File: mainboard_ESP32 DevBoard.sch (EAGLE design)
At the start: 42 parts, among them IC1 OP-AMP-2-LONG, IC2 OP-AMP-2-LONG, IC3 74HC08N, K1 AQH213, X1 JST-XH-02-PIN-LONG-PAD, X2 JST-XH-04-PIN-LONG-PAD, X3 1751248, X4 1751248, X5 JST-XH-04-PIN-LONG-PAD

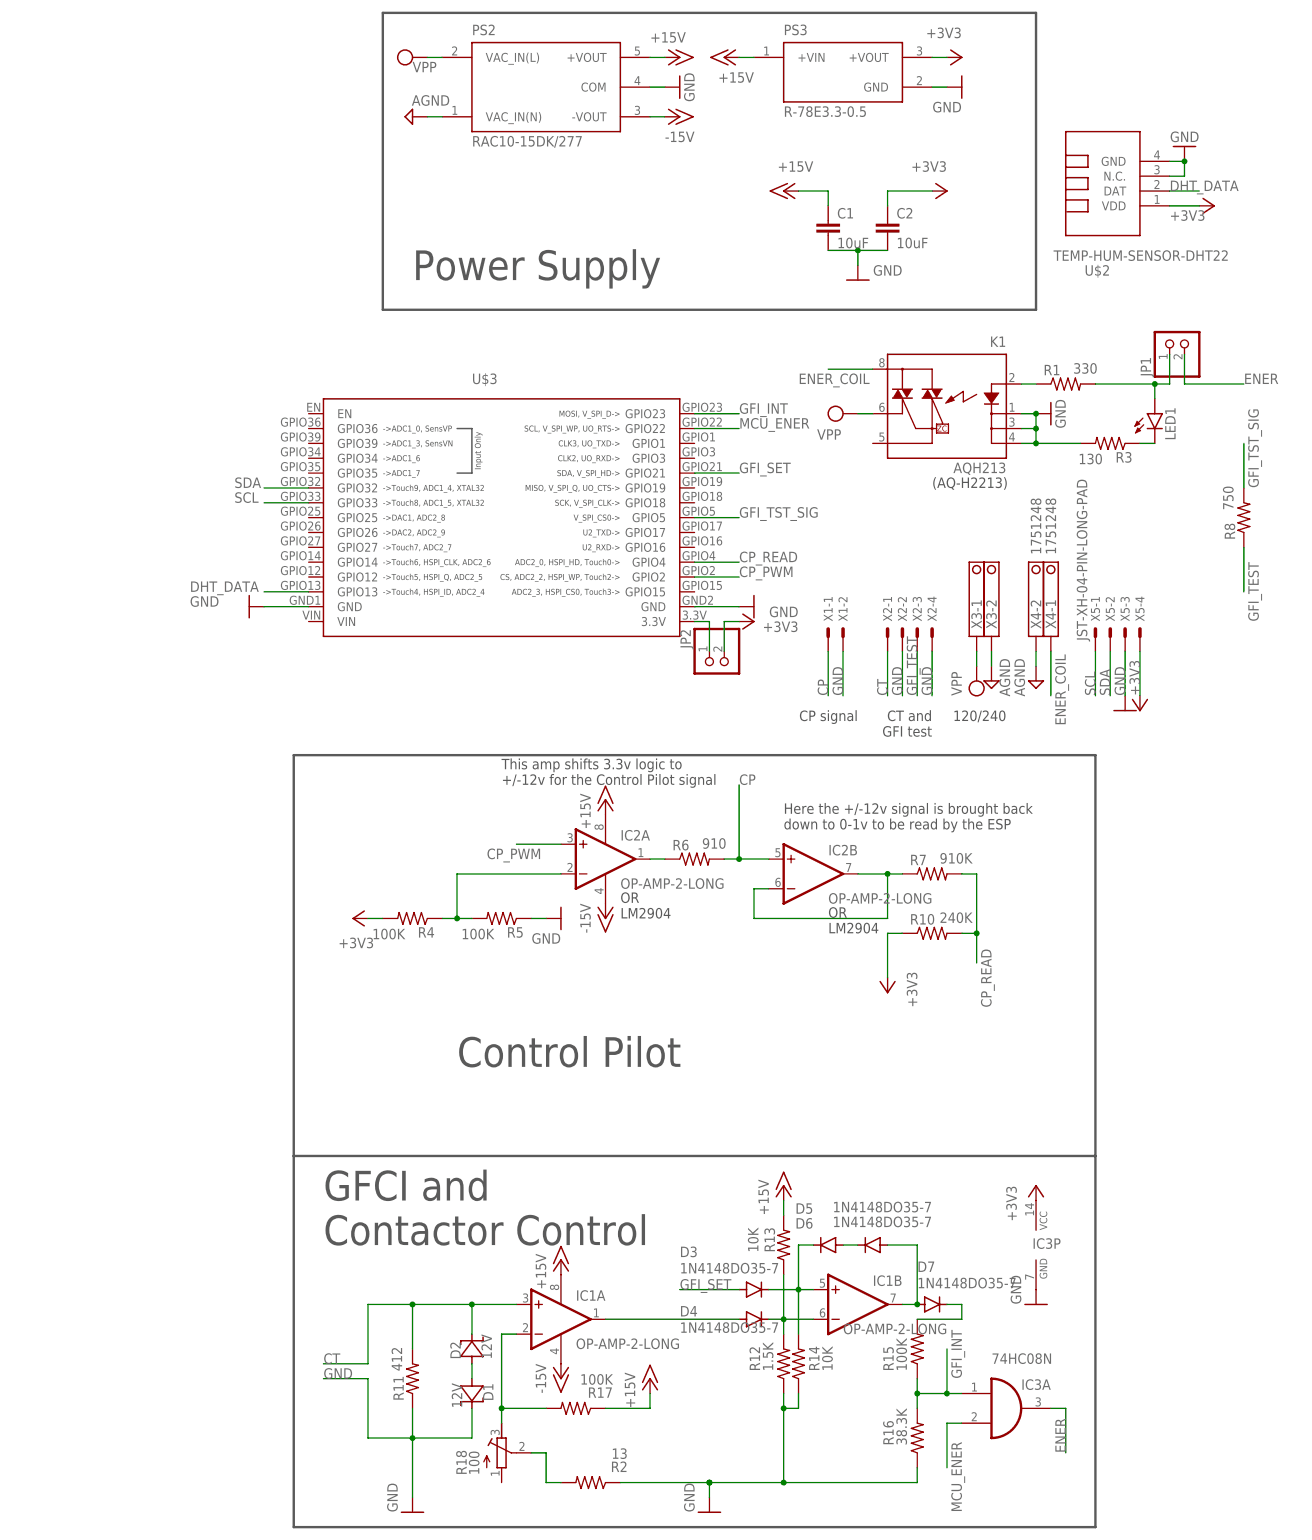
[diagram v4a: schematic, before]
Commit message: Updated ignore file. Made some adjustments after making the first board.
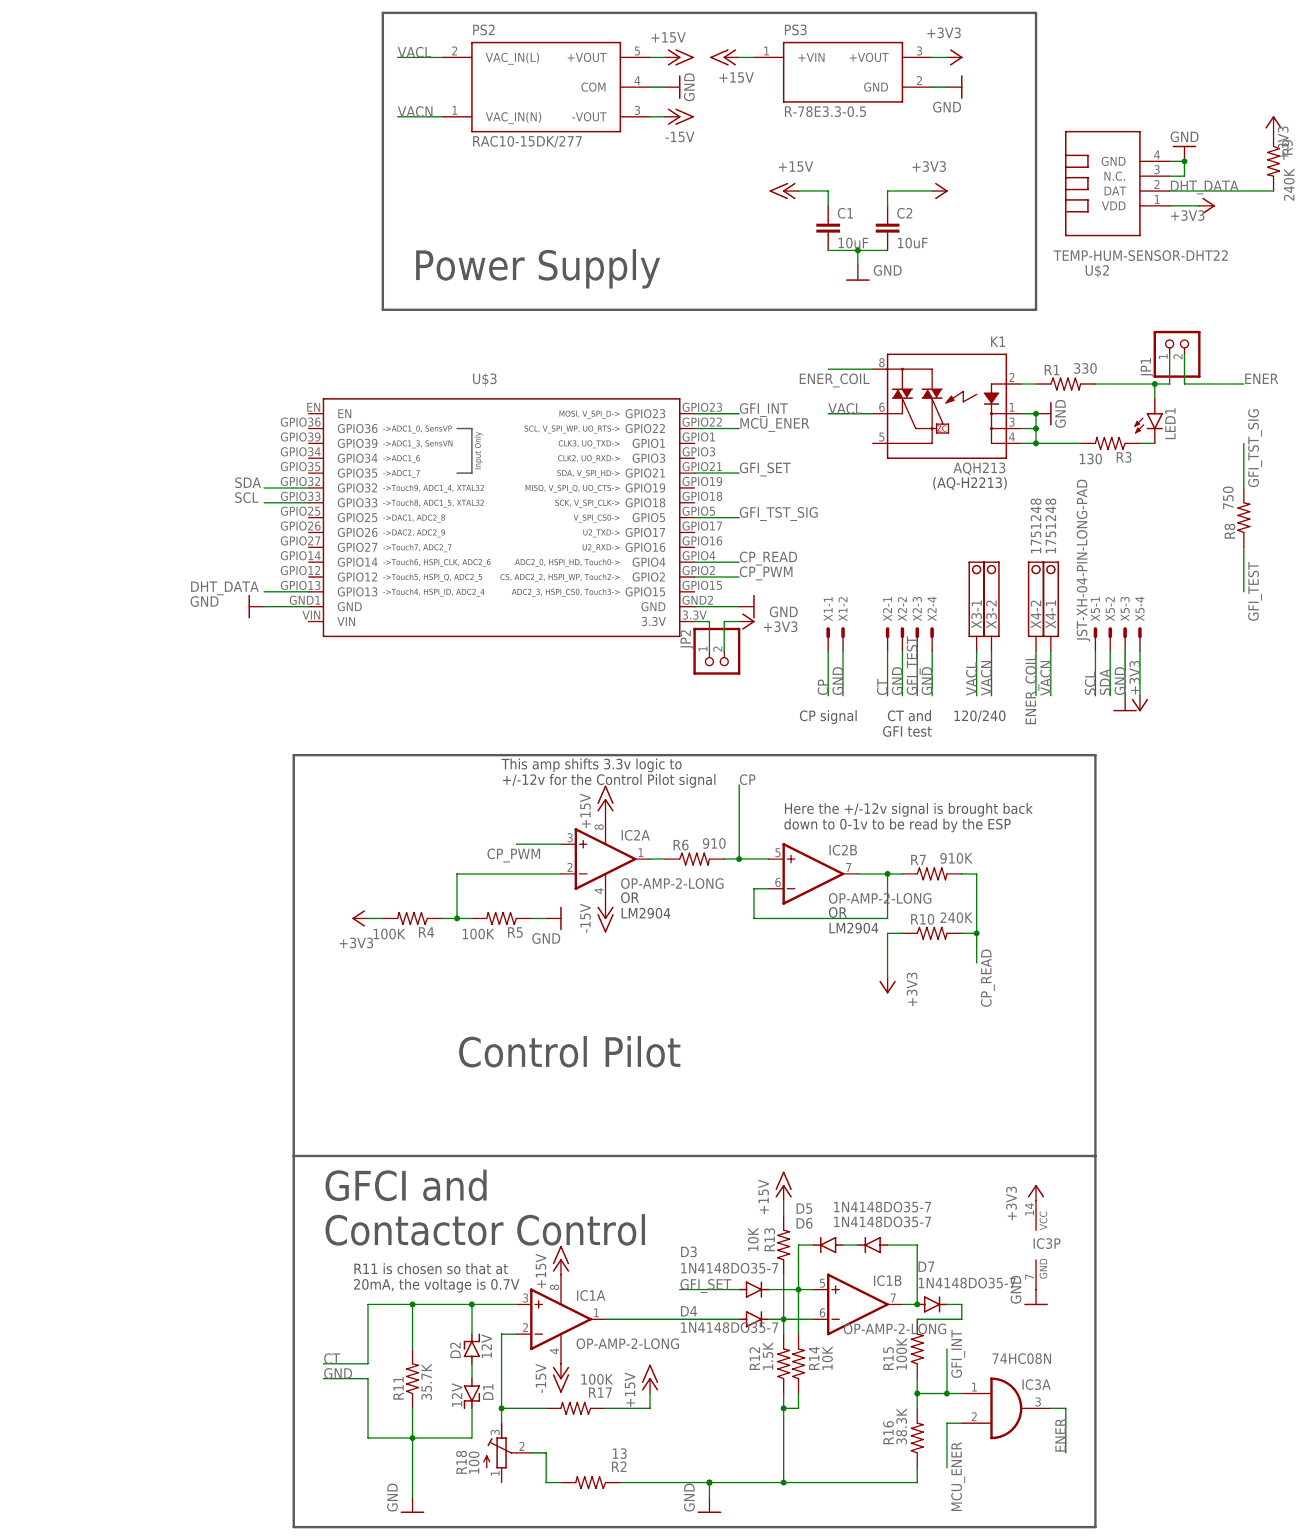
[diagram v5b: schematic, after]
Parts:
- added R9: 240K, Passive:RESISTORL
- R11: value 412 -> 35.7K
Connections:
- net VPP renamed VACL
- removed net AGND: PS2.VAC_IN(N), X3-2.K, X4-2.K
- new net VACN: PS2.VAC_IN(N), X3-2.K, X4-1.K
- net +3V3: now also R9.1
- net DHT_DATA: now also R9.2
- net ENER_COIL: now also X4-2.K; no longer X4-1.K
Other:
- note added: "R11 is chosen so that at 20mA, the voltage is 0.7V"
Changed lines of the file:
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@@
 <class number="0" name="default" width="0" drill="0">
+</class>
+<class number="1" name="Mains" width="0" drill="0">
+<clearance class="1" value="1.2"/>
 </class>
 </classes>
 <parts>
 <part name="K1" library="relay" library_urn="urn:adsk.eagle:library:339" deviceset="AQH*213" device="" package3d_urn="urn:adsk.eagle:package:24378/1" value="AQH213"/>
-<part name="SUPPLY1" library="supply2" library_urn="urn:adsk.eagle:library:372" deviceset="VPP" device=""/>
-<part name="SUPPLY2" library="supply2" library_urn="urn:adsk.eagle:library:372" deviceset="AGND" device=""/>
 <part name="R1" library="Passive" deviceset="RESISTOR" device="L" value="330"/>
 <part name="U$2" library="diy-modules" deviceset="TEMP-HUM-SENSOR-DHT22" device=""/>
@@
 <part name="PS2" library="RAC10-15DK_277" deviceset="RAC10-15DK/277" device=""/>
 <part name="GND10" library="supply1" library_urn="urn:adsk.eagle:library:371" deviceset="GND" device=""/>
-<part name="SUPPLY7" library="supply2" library_urn="urn:adsk.eagle:library:372" deviceset="VPP" device=""/>
-<part name="SUPPLY8" library="supply2" library_urn="urn:adsk.eagle:library:372" deviceset="AGND" device=""/>
 <part name="PS3" library="R-78E3.3-0.5" deviceset="R-78E3.3-0.5" device=""/>
 <part name="+3V5" library="supply1" library_urn="urn:adsk.eagle:library:371" deviceset="+3V3" device=""/>
@@
 <part name="D2" library="Passive" deviceset="ZENER" device="" value="12V"/>
 <part name="IC1" library="Op Amp" deviceset="OP-AMP-2" device="-LONG"/>
-<part name="R11" library="Passive" deviceset="RESISTOR" device="L" value="412"/>
+<part name="R11" library="Passive" deviceset="RESISTOR" device="L" value="35.7K"/>
 <part name="D3" library="diode" library_urn="urn:adsk.eagle:library:210" deviceset="1N4148" device="DO35-7" package3d_urn="urn:adsk.eagle:package:43339/2"/>
 <part name="D4" library="diode" library_urn="urn:adsk.eagle:library:210" deviceset="1N4148" device="DO35-7" package3d_urn="urn:adsk.eagle:package:43339/2"/>
@@
 <part name="X2" library="Rembrandt Electronics - JST XH Connectors v1-0" deviceset="JST-XH-04-PIN" device="-LONG-PAD"/>
 <part name="X3" library="con-phoenix-350" library_urn="urn:adsk.eagle:library:174" deviceset="1751248" device="" package3d_urn="urn:adsk.eagle:package:9395/1"/>
-<part name="SUPPLY5" library="supply2" library_urn="urn:adsk.eagle:library:372" deviceset="VPP" device=""/>
-<part name="SUPPLY6" library="supply2" library_urn="urn:adsk.eagle:library:372" deviceset="AGND" device=""/>
 <part name="X4" library="con-phoenix-350" library_urn="urn:adsk.eagle:library:174" deviceset="1751248" device="" package3d_urn="urn:adsk.eagle:package:9395/1"/>
 <part name="R2" library="Passive" deviceset="RESISTOR" device="L" value="13"/>
@@
 <part name="GND7" library="supply1" library_urn="urn:adsk.eagle:library:371" deviceset="GND" device=""/>
 <part name="+3V1" library="supply1" library_urn="urn:adsk.eagle:library:371" deviceset="+3V3" device=""/>
+<part name="R9" library="Passive" deviceset="RESISTOR" device="L" value="240K"/>
+<part name="+3V9" library="supply1" library_urn="urn:adsk.eagle:library:371" deviceset="+3V3" device=""/>
 </parts>
 <sheets>
@@
 <wire x1="119.38" y1="152.4" x2="7.62" y2="152.4" width="0.4064" layer="97"/>
 <text x="12.7" y="106.68" size="5.08" layer="97">Power Supply</text>
+<text x="2.54" y="-66.04" size="1.778" layer="97">R11 is chosen so that at
+20mA, the voltage is 0.7V</text>
 </plain>
 <instances>
@@
 <attribute name="VALUE" x="114.3" y="73.66" size="1.778" layer="96" font="vector" rot="MR0"/>
 </instance>
-<instance part="SUPPLY1" gate="G$1" x="86.36" y="83.82" smashed="yes" rot="R90">
-<attribute name="VALUE" x="81.915" y="79.375" size="1.778" layer="96"/>
-</instance>
-<instance part="SUPPLY2" gate="G$1" x="119.38" y="38.1" smashed="yes">
-<attribute name="VALUE" x="117.475" y="35.433" size="1.778" layer="96" rot="R90"/>
-</instance>
 <instance part="R1" gate="G$1" x="124.46" y="88.9" smashed="yes">
 <attribute name="NAME" x="120.65" y="90.3986" size="1.778" layer="95"/>
@@
 <attribute name="VALUE" x="60.96" y="137.16" size="1.778" layer="96" rot="R90"/>
 </instance>
-<instance part="SUPPLY7" gate="G$1" x="12.7" y="144.78" smashed="yes" rot="R90">
-<attribute name="VALUE" x="12.7" y="142.24" size="1.778" layer="96"/>
-</instance>
-<instance part="SUPPLY8" gate="G$1" x="12.7" y="134.62" smashed="yes" rot="R270">
-<attribute name="VALUE" x="12.573" y="136.525" size="1.778" layer="96"/>
-</instance>
 <instance part="PS3" gate="G$1" x="86.36" y="142.24" smashed="yes">
 <attribute name="NAME" x="76.1961" y="148.5979" size="1.77938125" layer="95"/>
@@
 <instance part="R11" gate="G$1" x="12.7" y="-81.28" smashed="yes" rot="R90">
 <attribute name="NAME" x="11.2014" y="-85.09" size="1.778" layer="95" rot="R90"/>
-<attribute name="VALUE" x="10.922" y="-80.01" size="1.778" layer="96" rot="R90"/>
+<attribute name="VALUE" x="16.002" y="-85.09" size="1.778" layer="96" rot="R90"/>
 </instance>
 <instance part="D3" gate="G$1" x="71.12" y="-66.04" smashed="yes">
@@
 <attribute name="NAME" x="112.649" y="46.99" size="1.778" layer="95" rot="R90"/>
 </instance>
-<instance part="SUPPLY5" gate="G$1" x="109.22" y="38.1" smashed="yes" rot="R180">
-<attribute name="VALUE" x="106.68" y="35.56" size="1.778" layer="96" rot="R90"/>
-</instance>
-<instance part="SUPPLY6" gate="G$1" x="111.76" y="38.1" smashed="yes">
-<attribute name="VALUE" x="114.935" y="35.433" size="1.778" layer="96" rot="R90"/>
-</instance>
 <instance part="X4" gate="-1" x="121.92" y="45.72" smashed="yes" rot="R90">
 <attribute name="NAME" x="122.809" y="46.99" size="1.778" layer="95" rot="R90"/>
@@
 <instance part="+3V1" gate="G$1" x="137.16" y="33.02" smashed="yes" rot="R180">
 <attribute name="VALUE" x="137.16" y="35.56" size="1.778" layer="96" rot="R90"/>
+</instance>
+<instance part="R9" gate="G$1" x="160.02" y="127" smashed="yes" rot="R270">
+<attribute name="NAME" x="161.5186" y="130.81" size="1.778" layer="95" rot="R270"/>
+<attribute name="VALUE" x="161.798" y="125.73" size="1.778" layer="96" rot="R270"/>
+</instance>
+<instance part="+3V9" gate="G$1" x="160.02" y="134.62" smashed="yes">
+<attribute name="VALUE" x="162.56" y="127" size="1.778" layer="96" rot="R90"/>
 </instance>
 </instances>
@@
 </busses>
 <nets>
-<net name="VPP" class="0">
-<segment>
-<pinref part="K1" gate="G$1" pin="DS3"/>
-<pinref part="SUPPLY1" gate="G$1" pin="VPP"/>
-<wire x1="91.44" y1="83.82" x2="88.9" y2="83.82" width="0.1524" layer="91"/>
-</segment>
-<segment>
-<pinref part="SUPPLY7" gate="G$1" pin="VPP"/>
-<pinref part="PS2" gate="G$1" pin="VAC_IN(L)"/>
-<wire x1="15.24" y1="144.78" x2="17.78" y2="144.78" width="0.1524" layer="91"/>
-</segment>
-<segment>
-<pinref part="X3" gate="-1" pin="K"/>
-<pinref part="SUPPLY5" gate="G$1" pin="VPP"/>
-<wire x1="109.22" y1="43.18" x2="109.22" y2="40.64" width="0.1524" layer="91"/>
-</segment>
-</net>
-<net name="AGND" class="0">
-<segment>
-<pinref part="SUPPLY8" gate="G$1" pin="AGND"/>
-<pinref part="PS2" gate="G$1" pin="VAC_IN(N)"/>
-<wire x1="15.24" y1="134.62" x2="17.78" y2="134.62" width="0.1524" layer="91"/>
-</segment>
-<segment>
-<pinref part="X3" gate="-2" pin="K"/>
-<pinref part="SUPPLY6" gate="G$1" pin="AGND"/>
-<wire x1="111.76" y1="43.18" x2="111.76" y2="40.64" width="0.1524" layer="91"/>
-</segment>
-<segment>
-<pinref part="SUPPLY2" gate="G$1" pin="AGND"/>
-<pinref part="X4" gate="-2" pin="K"/>
-<wire x1="119.38" y1="40.64" x2="119.38" y2="43.18" width="0.1524" layer="91"/>
-</segment>
-</net>
 <net name="N$1" class="0">
 <segment>
@@
 <pinref part="+3V1" gate="G$1" pin="+3V3"/>
 </segment>
+<segment>
+<pinref part="R9" gate="G$1" pin="1"/>
+<pinref part="+3V9" gate="G$1" pin="+3V3"/>
+</segment>
 </net>
 <net name="+15V" class="0">
@@
 </segment>
 </net>
-<net name="ENER_COIL" class="0">
+<net name="ENER_COIL" class="1">
 <segment>
 <pinref part="K1" gate="G$1" pin="DS1"/>
@@
 </segment>
 <segment>
-<pinref part="X4" gate="-1" pin="K"/>
-<wire x1="121.92" y1="43.18" x2="121.92" y2="35.56" width="0.1524" layer="91"/>
-<label x="124.46" y="30.48" size="1.778" layer="95" rot="R90"/>
+<pinref part="X4" gate="-2" pin="K"/>
+<wire x1="119.38" y1="43.18" x2="119.38" y2="35.56" width="0.1524" layer="91"/>
+<label x="119.38" y="30.48" size="1.778" layer="95" rot="R90"/>
 </segment>
 </net>
@@
 <segment>
 <pinref part="U$2" gate="G$1" pin="DAT"/>
-<wire x1="142.24" y1="121.92" x2="147.32" y2="121.92" width="0.1524" layer="91"/>
 <label x="142.24" y="121.92" size="1.778" layer="95"/>
+<pinref part="R9" gate="G$1" pin="2"/>
+<wire x1="142.24" y1="121.92" x2="160.02" y2="121.92" width="0.1524" layer="91"/>
 </segment>
 </net>
@@
 </segment>
 </net>
+<net name="VACL" class="1">
+<segment>
+<pinref part="PS2" gate="G$1" pin="VAC_IN(L)"/>
+<wire x1="17.78" y1="144.78" x2="10.16" y2="144.78" width="0.1524" layer="91"/>
+<label x="10.16" y="144.78" size="1.778" layer="95"/>
+</segment>
+<segment>
+<pinref part="X3" gate="-1" pin="K"/>
+<wire x1="109.22" y1="43.18" x2="109.22" y2="35.56" width="0.1524" layer="91"/>
+<label x="109.22" y="35.56" size="1.778" layer="95" rot="R90"/>
+</segment>
+<segment>
+<pinref part="K1" gate="G$1" pin="DS3"/>
+<wire x1="91.44" y1="83.82" x2="83.82" y2="83.82" width="0.1524" layer="91"/>
+<label x="83.82" y="83.82" size="1.778" layer="95"/>
+</segment>
+</net>
+<net name="VACN" class="1">
+<segment>
+<pinref part="PS2" gate="G$1" pin="VAC_IN(N)"/>
+<wire x1="17.78" y1="134.62" x2="10.16" y2="134.62" width="0.1524" layer="91"/>
+<label x="10.16" y="134.62" size="1.778" layer="95"/>
+</segment>
+<segment>
+<pinref part="X3" gate="-2" pin="K"/>
+<wire x1="111.76" y1="43.18" x2="111.76" y2="35.56" width="0.1524" layer="91"/>
+<label x="111.76" y="35.56" size="1.778" layer="95" rot="R90"/>
+</segment>
+<segment>
+<pinref part="X4" gate="-1" pin="K"/>
+<wire x1="121.92" y1="43.18" x2="121.92" y2="35.56" width="0.1524" layer="91"/>
+<label x="121.92" y="35.56" size="1.778" layer="95" rot="R90"/>
+</segment>
+</net>
